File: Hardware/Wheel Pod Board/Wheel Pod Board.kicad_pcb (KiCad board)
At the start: 2 copper layers, 90 x 25.5 mm, 30 parts, among them J1 Conn_RJ-45, P1 UIM240XX_Stepper_Conn, P2 RS232, P3 ST_SWD_Connector, P4 SyRen, P5 BATT, U1 STM32F401RCT6, U2 SN75176BDR, U3 ZXCT1107, U4 ZXCT1107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

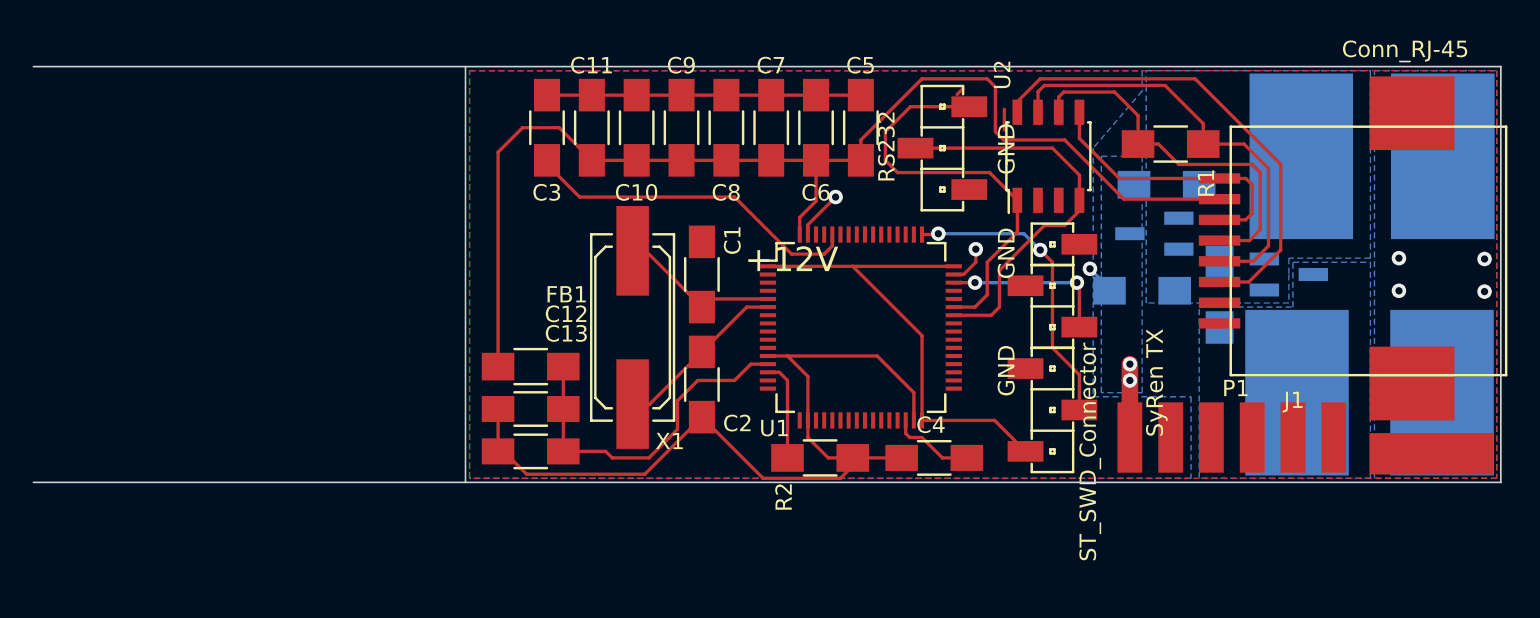
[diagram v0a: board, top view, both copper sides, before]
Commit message: Finish PCB reroute one
Resolve #8, resolve #13
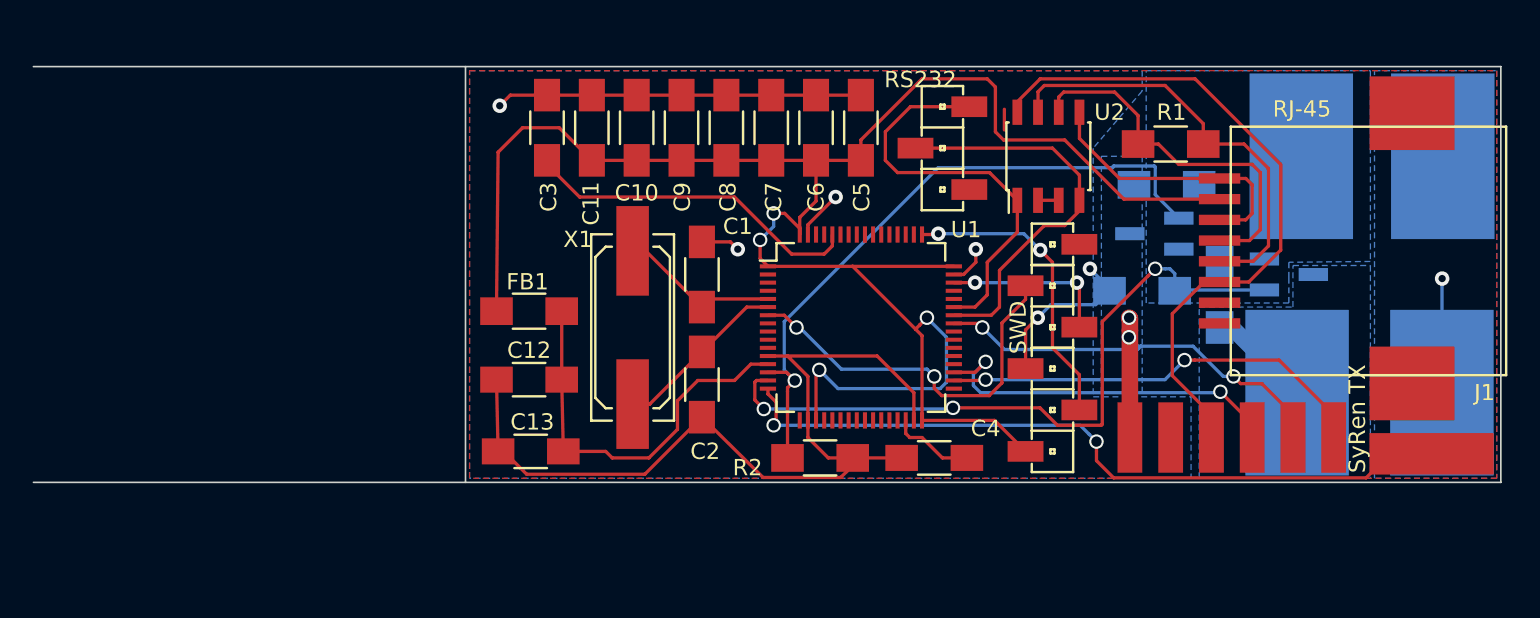
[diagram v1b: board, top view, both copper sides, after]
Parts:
- J1: value Conn_RJ-45 -> RJ-45
- P3: value ST_SWD_Connector -> SWD
- moved FB1 3.40 mm to (223.6, 143.8)
- moved C12 1.80 mm to (223.6, 148.0)
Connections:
- J1 pad : (no net) -> GND
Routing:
- net /USART2_TX: track 0.00 -> 45.5 mm, vias 0 -> 2
- net /SyRenCurrent: track 0.00 -> 42.8 mm, vias 0 -> 3
- net /StepperCurrent: track 6.16 -> 41.2 mm, vias 0 -> 1
- net /Step_Enable: track 0.00 -> 26.6 mm, vias 0 -> 2
- net /Step_Step: track 0.00 -> 25.1 mm, vias 0 -> 2
- net /NRST: track 0.00 -> 23.7 mm, vias 0 -> 2
- net /Step_Direction: track 0.00 -> 22.9 mm, vias 0 -> 2
- net GND: track 96.7 -> 119.5 mm
- net +3V3: track 101.0 -> 120.9 mm, vias 0 -> 4
- net +5V: track 29.4 -> 41.7 mm
- net Net-(P4-Pad2): track 0.00 -> 6.41 mm
- net /VDDA: track 21.3 -> 24.7 mm
- net /Stp+12V: track 4.50 -> 7.82 mm
- net Net-(U2-Pad2): track 0.00 -> 1.27 mm
- net (no net): track 1.79 -> 1.27 mm
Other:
- board text removed: "+12V"
- board text removed: "GND"

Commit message: Attach 485 TX enable to micro
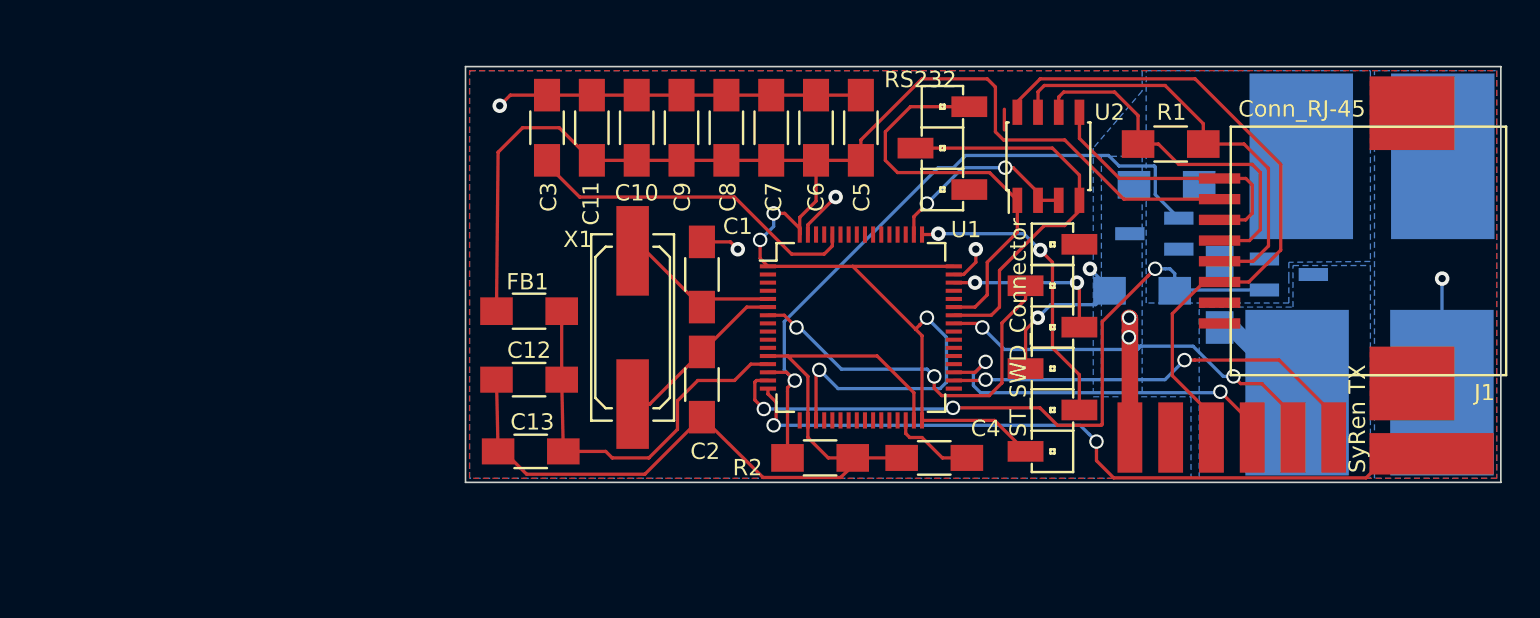
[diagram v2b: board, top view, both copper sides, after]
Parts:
- J1: value RJ-45 -> Conn_RJ-45
- P3: value SWD -> ST_SWD_Connector
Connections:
- J1 pad : GND -> (no net)
- U1 pad 50: Net-(U1-Pad50) -> /TX_EN
- U2 pad 2: Net-(U2-Pad2) -> /TX_EN
- U2 pad 3: Net-(U2-Pad2) -> /TX_EN
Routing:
- net /TX_EN: track 0.00 -> 12.3 mm, vias 0 -> 2
- net Net-(U2-Pad2): track 1.27 -> 0.00 mm
- net /StepperCurrent: track 41.2 -> 41.7 mm
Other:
- board size 90 x 25.5 mm -> 63.5 x 25.5 mm
